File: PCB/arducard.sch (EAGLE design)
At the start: 97 parts, among them J1 USB MICRO, J2 microSD, J3 051296-4094, J4 M02PTH, Q1 BSS84, Q10 DMG2301U-7, Q2 BC817-16LT1SMD, Q3 DMG2301U-7, Q4 2N7002, Q5 BSS84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

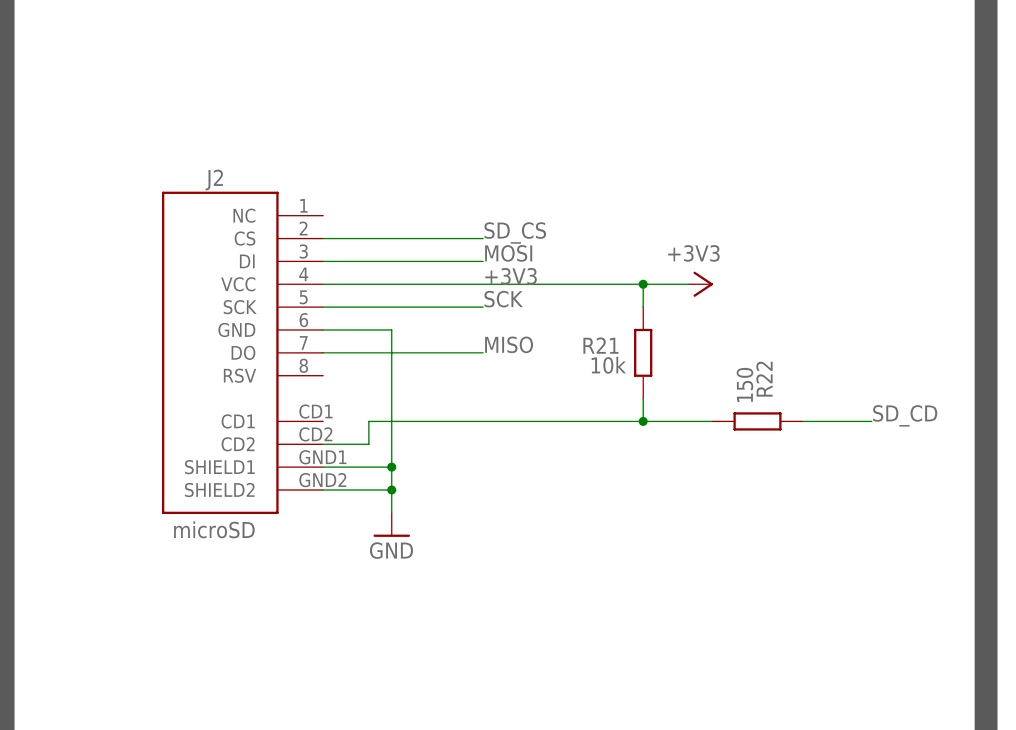
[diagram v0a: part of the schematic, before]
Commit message: removed microsd
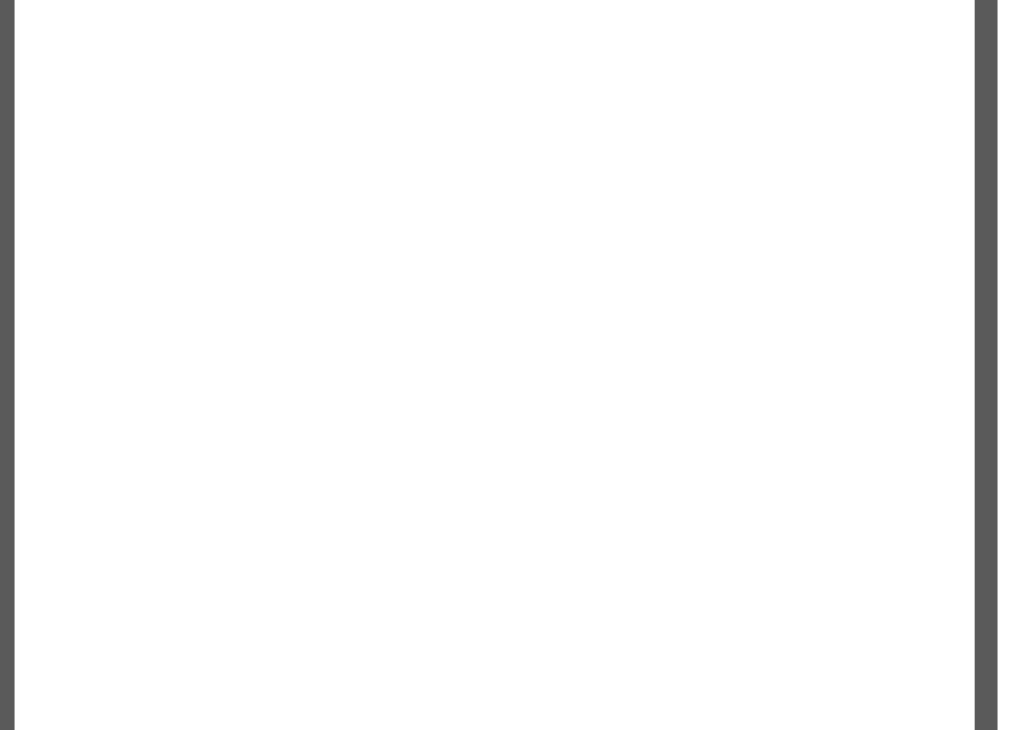
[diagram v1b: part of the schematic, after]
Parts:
- removed J2: microSD, SparkFun:USD-SOCKETSMD
- removed R21: 10k, SmartPrj:R-EU_R0603
- removed R22: 150, SmartPrj:R-EU_R0603
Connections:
- removed net CDP: J2.CD2, R21.1, R22.1
- net +3V3: no longer J2.VCC, R21.2
- net GND: no longer J2.GND, J2.SHIELD1, J2.SHIELD2
- net MISO: no longer J2.DO
- net MOSI: no longer J2.DI
- net SCK: no longer J2.SCK
- net SD_CD: no longer R22.2
- net SD_CS: no longer J2.CS
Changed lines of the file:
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@@
 <part name="+3V3" library="supply1" deviceset="+3V3" device=""/>
 <part name="U1" library="SmartPrj" deviceset="ATMEGA32U4-XU" device="AU"/>
-<part name="J2" library="SparkFun" deviceset="USD-SOCKET" device="SMD" value="microSD"/>
-<part name="R21" library="SmartPrj" deviceset="R-EU_" device="R0603" value="10k"/>
 <part name="C14" library="SmartPrj" deviceset="C-EU" device="C0603" value="1uF"/>
 <part name="+3V4" library="supply1" deviceset="+3V3" device=""/>
@@
 <part name="C11" library="SmartPrj" deviceset="C-EU" device="C0603" value="10 uF"/>
 <part name="+3V5" library="supply1" deviceset="+3V3" device=""/>
-<part name="+3V6" library="supply1" deviceset="+3V3" device=""/>
 <part name="SW0" library="arducard-switch" deviceset="EVQ-PUA" device=""/>
 <part name="R14" library="SmartPrj" deviceset="R-EU_" device="R0603" value="150"/>
@@
 <part name="R17" library="SmartPrj" deviceset="R-EU_" device="R0603" value="150"/>
 <part name="R12" library="SmartPrj" deviceset="R-EU_" device="R0603" value="10k"/>
-<part name="R22" library="SmartPrj" deviceset="R-EU_" device="R0603" value="150"/>
 <part name="C7" library="SmartPrj" deviceset="C-EU" device="C0603" value="100nF"/>
 <part name="C5" library="SmartPrj" deviceset="C-EU" device="C0603" value="1uF"/>
 <part name="GND3" library="supply1" deviceset="GND" device=""/>
 <part name="GND5" library="supply1" deviceset="GND" device=""/>
-<part name="GND7" library="supply1" deviceset="GND" device=""/>
 <part name="GND11" library="supply1" deviceset="GND" device=""/>
 <part name="GND13" library="supply1" deviceset="GND" device=""/>
@@
 <instance part="+3V3" gate="G$1" x="175.26" y="243.84" rot="R270"/>
 <instance part="U1" gate="G$1" x="139.7" y="93.98"/>
-<instance part="J2" gate="G$1" x="627.38" y="241.3" smashed="yes" rot="MR0">
-<attribute name="NAME" x="622.046" y="257.302" size="1.778" layer="95"/>
-<attribute name="VALUE" x="618.236" y="218.186" size="1.778" layer="96"/>
-</instance>
-<instance part="R21" gate="G$1" x="670.56" y="238.76" smashed="yes" rot="R90">
-<attribute name="NAME" x="668.02" y="240.4364" size="1.778" layer="95" rot="R180"/>
-<attribute name="VALUE" x="668.655" y="238.252" size="1.778" layer="96" rot="R180"/>
-</instance>
 <instance part="C14" gate="G$1" x="335.28" y="254"/>
 <instance part="+3V4" gate="G$1" x="45.72" y="142.24"/>
@@
 <instance part="C11" gate="G$1" x="581.66" y="238.76"/>
 <instance part="+3V5" gate="G$1" x="594.36" y="248.92" rot="R270"/>
-<instance part="+3V6" gate="G$1" x="678.18" y="246.38" rot="R270"/>
 <instance part="SW0" gate="G$1" x="60.96" y="264.16"/>
 <instance part="R14" gate="G$1" x="33.02" y="264.16" smashed="yes">
@@
 <attribute name="VALUE" x="60.452" y="230.505" size="1.778" layer="96" rot="R90"/>
 </instance>
-<instance part="R22" gate="G$1" x="683.26" y="231.14" smashed="yes">
-<attribute name="NAME" x="684.9364" y="233.68" size="1.778" layer="95" rot="R90"/>
-<attribute name="VALUE" x="682.752" y="233.045" size="1.778" layer="96" rot="R90"/>
-</instance>
 <instance part="C7" gate="G$1" x="55.88" y="78.74"/>
 <instance part="C5" gate="G$1" x="45.72" y="83.82"/>
 <instance part="GND3" gate="1" x="45.72" y="73.66"/>
 <instance part="GND5" gate="1" x="127" y="228.6" rot="R270"/>
-<instance part="GND7" gate="1" x="642.62" y="218.44"/>
 <instance part="GND11" gate="1" x="546.1" y="228.6"/>
 <instance part="GND13" gate="1" x="581.66" y="228.6"/>
@@
 <pinref part="GND5" gate="1" pin="GND"/>
 <pinref part="U3" gate="G$1" pin="GND"/>
-</segment>
-<segment>
-<pinref part="J2" gate="G$1" pin="GND"/>
-<wire x1="635" y1="241.3" x2="642.62" y2="241.3" width="0.1524" layer="91"/>
-<pinref part="J2" gate="G$1" pin="SHIELD1"/>
-<wire x1="635" y1="226.06" x2="642.62" y2="226.06" width="0.1524" layer="91"/>
-<wire x1="642.62" y1="226.06" x2="642.62" y2="241.3" width="0.1524" layer="91"/>
-<pinref part="J2" gate="G$1" pin="SHIELD2"/>
-<wire x1="635" y1="223.52" x2="642.62" y2="223.52" width="0.1524" layer="91"/>
-<wire x1="642.62" y1="223.52" x2="642.62" y2="226.06" width="0.1524" layer="91"/>
-<junction x="642.62" y="226.06"/>
-<wire x1="642.62" y1="220.98" x2="642.62" y2="223.52" width="0.1524" layer="91"/>
-<junction x="642.62" y="223.52"/>
-<pinref part="GND7" gate="1" pin="GND"/>
 </segment>
 <segment>
@@
 </segment>
 <segment>
-<pinref part="J2" gate="G$1" pin="SCK"/>
-<wire x1="635" y1="243.84" x2="652.78" y2="243.84" width="0.1524" layer="91"/>
-<label x="652.78" y="243.84" size="1.778" layer="95"/>
-</segment>
-<segment>
 <pinref part="U1" gate="G$1" pin="(SCLK/PCINT1)PB1"/>
 <wire x1="175.26" y1="101.6" x2="187.96" y2="101.6" width="0.1524" layer="91"/>
@@
 </segment>
 <segment>
-<pinref part="J2" gate="G$1" pin="DO"/>
-<wire x1="635" y1="238.76" x2="652.78" y2="238.76" width="0.1524" layer="91"/>
-<label x="652.78" y="238.76" size="1.778" layer="95"/>
-</segment>
-<segment>
 <pinref part="U1" gate="G$1" pin="(PD0/MISO/PCINT3)PB3"/>
 <wire x1="175.26" y1="106.68" x2="187.96" y2="106.68" width="0.1524" layer="91"/>
@@
 <label x="175.26" y="228.6" size="1.778" layer="95"/>
 <pinref part="U3" gate="G$1" pin="SI"/>
-</segment>
-<segment>
-<pinref part="J2" gate="G$1" pin="DI"/>
-<wire x1="635" y1="248.92" x2="652.78" y2="248.92" width="0.1524" layer="91"/>
-<label x="652.78" y="248.92" size="1.778" layer="95"/>
 </segment>
 <segment>
@@
 <junction x="574.04" y="248.92"/>
 <pinref part="U2" gate="G1" pin="BYP"/>
-</segment>
-<segment>
-<pinref part="J2" gate="G$1" pin="VCC"/>
-<wire x1="635" y1="246.38" x2="670.56" y2="246.38" width="0.1524" layer="91"/>
-<wire x1="670.56" y1="246.38" x2="670.56" y2="243.84" width="0.1524" layer="91"/>
-<pinref part="R21" gate="G$1" pin="2"/>
-<label x="652.78" y="246.38" size="1.778" layer="95"/>
-<pinref part="+3V6" gate="G$1" pin="+3V3"/>
-<wire x1="670.56" y1="246.38" x2="675.64" y2="246.38" width="0.1524" layer="91"/>
-<junction x="670.56" y="246.38"/>
 </segment>
 <segment>
@@
 </segment>
 </net>
-<net name="CDP" class="0">
-<segment>
-<pinref part="R21" gate="G$1" pin="1"/>
-<wire x1="640.08" y1="231.14" x2="670.56" y2="231.14" width="0.1524" layer="91"/>
-<wire x1="670.56" y1="231.14" x2="678.18" y2="231.14" width="0.1524" layer="91"/>
-<wire x1="670.56" y1="231.14" x2="670.56" y2="233.68" width="0.1524" layer="91"/>
-<junction x="670.56" y="231.14"/>
-<pinref part="R22" gate="G$1" pin="1"/>
-<pinref part="J2" gate="G$1" pin="CD2"/>
-<wire x1="635" y1="228.6" x2="640.08" y2="228.6" width="0.1524" layer="91"/>
-<wire x1="640.08" y1="228.6" x2="640.08" y2="231.14" width="0.1524" layer="91"/>
-</segment>
-</net>
 <net name="SD_CS" class="0">
-<segment>
-<pinref part="J2" gate="G$1" pin="CS"/>
-<wire x1="635" y1="251.46" x2="652.78" y2="251.46" width="0.1524" layer="91"/>
-<label x="652.78" y="251.46" size="1.778" layer="95"/>
-</segment>
 <segment>
 <pinref part="U1" gate="G$1" pin="(XCK1/#CTS)PD5"/>
@@
 <net name="SD_CD" class="0">
 <segment>
-<pinref part="R22" gate="G$1" pin="2"/>
-<wire x1="688.34" y1="231.14" x2="695.96" y2="231.14" width="0.1524" layer="91"/>
-<label x="695.96" y="231.14" size="1.778" layer="95"/>
-</segment>
-<segment>
 <pinref part="U1" gate="G$1" pin="(PCINT5/OC1A/#OC4B/ADC12)PB5"/>

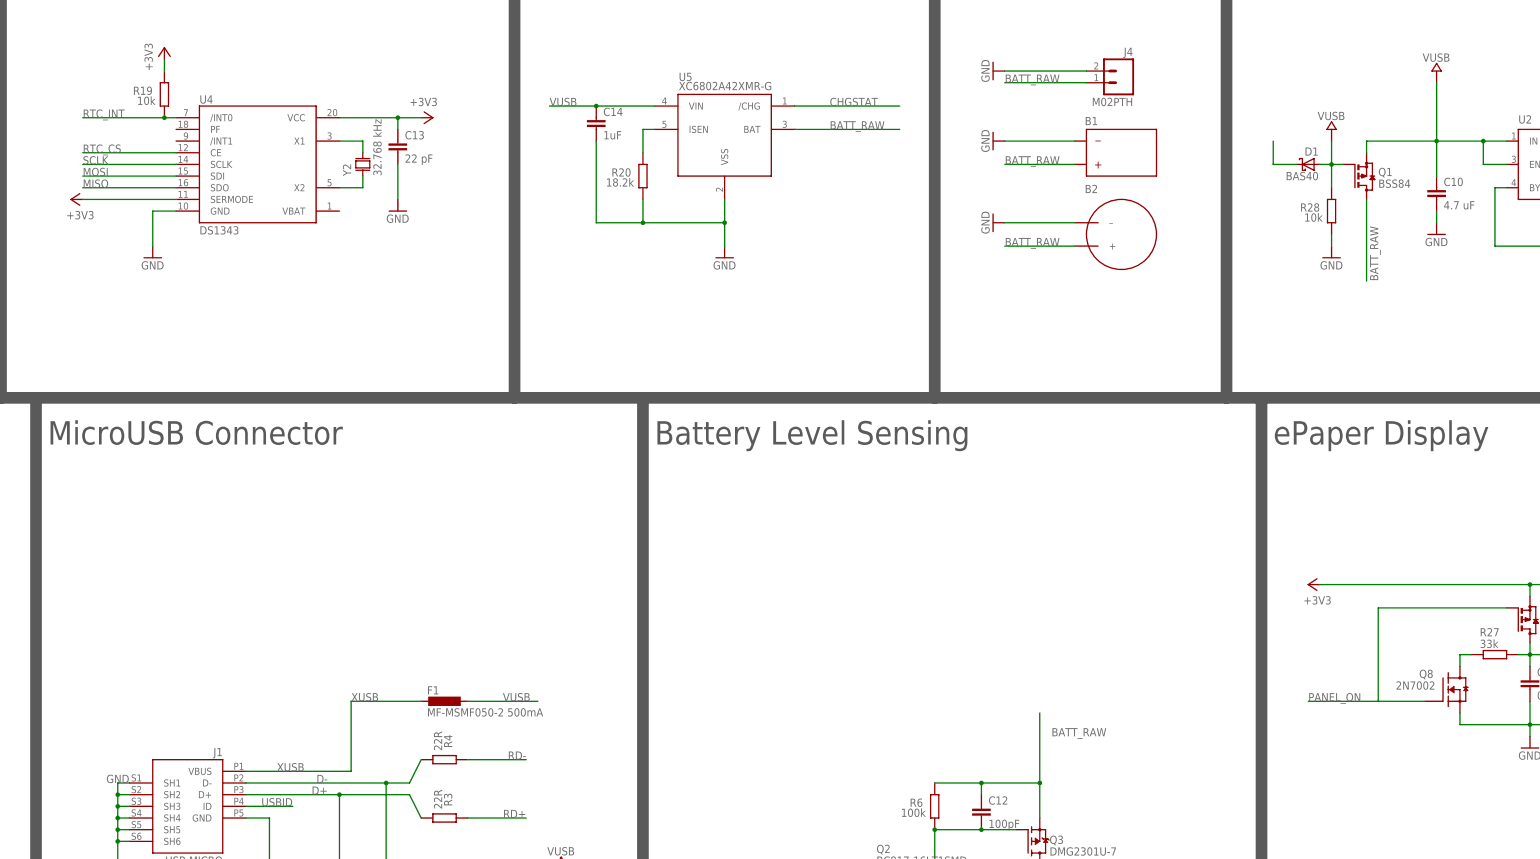
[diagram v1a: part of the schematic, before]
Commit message: fixed VUSB diode
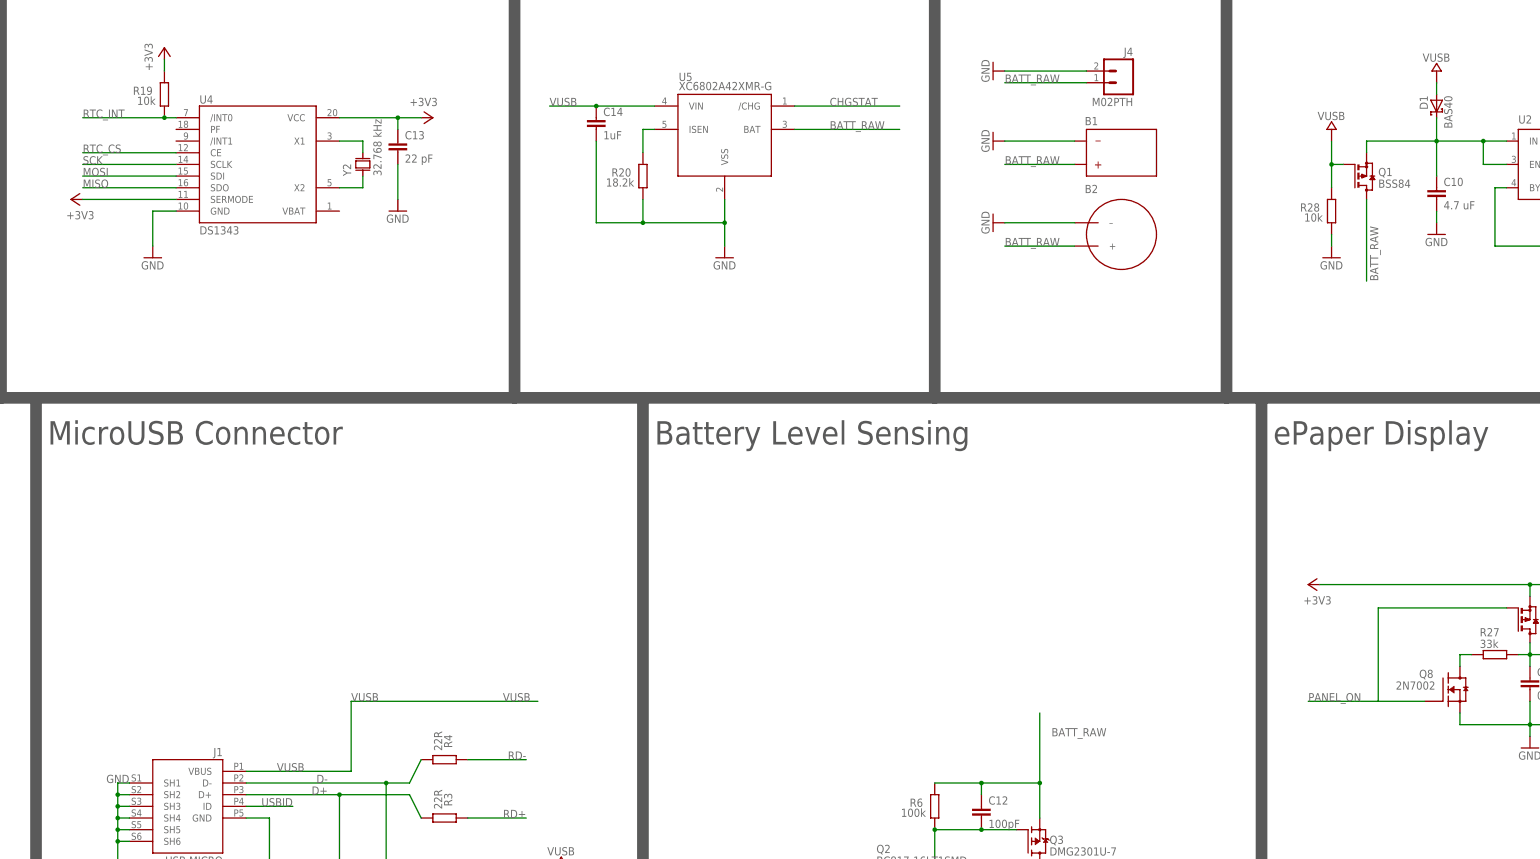
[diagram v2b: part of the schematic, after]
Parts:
- removed F1: MF-MSMF050-2 500mA, rcl:L-EUL1812
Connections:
- removed net SCLK: U4.SCLK
- removed net XUSB: F1.2, J1.VBUS
- net N$10: now also C10.1, Q1.S, U2.EN, U2.IN
- net SCK: now also U4.SCLK
- net VUSB: now also J1.VBUS; no longer C10.1, F1.1, Q1.S, U2.EN, U2.IN
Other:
- moved on the sheet: D1
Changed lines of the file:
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@@
 <part name="GND18" library="supply1" deviceset="GND" device=""/>
 <part name="Y1" library="SmartPrj" deviceset="CRYSTAL-3.2-2.5" device="" value="8MHz KX-7"/>
-<part name="F1" library="rcl" deviceset="L-EU" device="L1812" value="MF-MSMF050-2 500mA"/>
 <part name="Z1" library="varistor" deviceset="VARISTOR" device="CN0603" value="CG0603MLC-05E"/>
 <part name="Z2" library="varistor" deviceset="VARISTOR" device="CN0603" value="CG0603MLC-05E"/>
@@
 <attribute name="VALUE" x="38.1" y="96.52" size="1.778" layer="96"/>
 </instance>
-<instance part="F1" gate="G$1" x="302.26" y="127" rot="R270"/>
 <instance part="Z1" gate="G$1" x="279.4" y="76.2" smashed="yes" rot="R90">
 <attribute name="NAME" x="276.86" y="73.66" size="1.778" layer="95" rot="R90"/>
@@
 <instance part="Q1" gate="G$1" x="502.92" y="241.3"/>
 <instance part="U$12" gate="G$1" x="518.16" y="264.16"/>
-<instance part="D1" gate="1" x="490.22" y="243.84" rot="MR0"/>
+<instance part="D1" gate="1" x="518.16" y="256.54" rot="MR270"/>
 <instance part="U3" gate="G$1" x="152.4" y="238.76"/>
 <instance part="U5" gate="XC6802A42XMR-G" x="363.22" y="254"/>
@@
 <pinref part="J3" gate="G$1" pin="SCLK"/>
 </segment>
+<segment>
+<pinref part="U4" gate="G$1" pin="SCLK"/>
+<wire x1="243.84" y1="243.84" x2="223.52" y2="243.84" width="0.1524" layer="91"/>
+<label x="223.52" y="243.84" size="1.778" layer="95"/>
+</segment>
 </net>
 <net name="MISO" class="0">
@@
 </segment>
 </net>
-<net name="VUSB" class="0">
+<net name="VUSB" class="3">
 <segment>
 <wire x1="114.3" y1="60.96" x2="104.14" y2="60.96" width="0.1524" layer="91"/>
@@
 </segment>
 <segment>
-<wire x1="322.58" y1="127" x2="307.34" y2="127" width="0.1524" layer="91"/>
-<label x="314.96" y="127" size="1.778" layer="95"/>
-<pinref part="F1" gate="G$1" pin="1"/>
-</segment>
-<segment>
 <wire x1="347.98" y1="256.54" x2="335.28" y2="256.54" width="0.1524" layer="91"/>
 <pinref part="C14" gate="G$1" pin="1"/>
@@
 </segment>
 <segment>
-<wire x1="528.32" y1="248.92" x2="533.4" y2="248.92" width="0.1524" layer="91"/>
-<wire x1="533.4" y1="243.84" x2="528.32" y2="243.84" width="0.1524" layer="91"/>
-<wire x1="528.32" y1="243.84" x2="528.32" y2="248.92" width="0.1524" layer="91"/>
-<wire x1="528.32" y1="248.92" x2="518.16" y2="248.92" width="0.1524" layer="91"/>
-<junction x="528.32" y="248.92"/>
-<pinref part="C10" gate="G$1" pin="1"/>
-<wire x1="518.16" y1="241.3" x2="518.16" y2="248.92" width="0.1524" layer="91"/>
-<junction x="518.16" y="248.92"/>
-<pinref part="U$12" gate="G$1" pin="VUSB"/>
-<wire x1="518.16" y1="248.92" x2="518.16" y2="261.62" width="0.1524" layer="91"/>
-<pinref part="U2" gate="G1" pin="IN"/>
-<pinref part="U2" gate="G1" pin="EN"/>
-<pinref part="Q1" gate="G$1" pin="S"/>
-<wire x1="502.92" y1="246.38" x2="502.92" y2="248.92" width="0.1524" layer="91"/>
-<wire x1="502.92" y1="248.92" x2="518.16" y2="248.92" width="0.1524" layer="91"/>
-</segment>
-<segment>
-<pinref part="D1" gate="1" pin="A"/>
 <pinref part="Q1" gate="G$1" pin="G"/>
-<wire x1="492.76" y1="243.84" x2="495.3" y2="243.84" width="0.1524" layer="91"/>
 <pinref part="R28" gate="G$1" pin="2"/>
 <wire x1="495.3" y1="243.84" x2="497.84" y2="243.84" width="0.1524" layer="91"/>
@@
 <wire x1="495.3" y1="243.84" x2="495.3" y2="248.92" width="0.1524" layer="91"/>
 <junction x="495.3" y="243.84"/>
+</segment>
+<segment>
+<pinref part="D1" gate="1" pin="A"/>
+<pinref part="U$12" gate="G$1" pin="VUSB"/>
+<wire x1="518.16" y1="259.08" x2="518.16" y2="261.62" width="0.1524" layer="91"/>
+</segment>
+<segment>
+<wire x1="281.94" y1="111.76" x2="281.94" y2="127" width="0.1524" layer="91"/>
+<wire x1="281.94" y1="127" x2="322.58" y2="127" width="0.1524" layer="91"/>
+<wire x1="259.08" y1="111.76" x2="281.94" y2="111.76" width="0.1524" layer="91"/>
+<label x="271.78" y="111.76" size="1.778" layer="95" rot="MR0"/>
+<label x="281.94" y="127" size="1.778" layer="95"/>
+<pinref part="J1" gate="G$1" pin="VBUS"/>
+<label x="314.96" y="127" size="1.778" layer="95"/>
 </segment>
 </net>
@@
 <pinref part="J1" gate="G$1" pin="D+"/>
 <pinref part="R3" gate="G$1" pin="1"/>
-</segment>
-</net>
-<net name="XUSB" class="3">
-<segment>
-<wire x1="281.94" y1="111.76" x2="281.94" y2="127" width="0.1524" layer="91"/>
-<wire x1="281.94" y1="127" x2="297.18" y2="127" width="0.1524" layer="91"/>
-<wire x1="259.08" y1="111.76" x2="281.94" y2="111.76" width="0.1524" layer="91"/>
-<label x="271.78" y="111.76" size="1.778" layer="95" rot="MR0"/>
-<label x="281.94" y="127" size="1.778" layer="95"/>
-<pinref part="F1" gate="G$1" pin="2"/>
-<pinref part="J1" gate="G$1" pin="VBUS"/>
 </segment>
 </net>
@@
 </segment>
 </net>
-<net name="SCLK" class="0">
-<segment>
-<pinref part="U4" gate="G$1" pin="SCLK"/>
-<wire x1="243.84" y1="243.84" x2="223.52" y2="243.84" width="0.1524" layer="91"/>
-<label x="223.52" y="243.84" size="1.778" layer="95"/>
-</segment>
-</net>
 <net name="N$10" class="0">
 <segment>
-<wire x1="482.6" y1="248.92" x2="482.6" y2="243.84" width="0.1524" layer="91"/>
+<wire x1="528.32" y1="248.92" x2="533.4" y2="248.92" width="0.1524" layer="91"/>
+<wire x1="533.4" y1="243.84" x2="528.32" y2="243.84" width="0.1524" layer="91"/>
+<wire x1="528.32" y1="243.84" x2="528.32" y2="248.92" width="0.1524" layer="91"/>
+<wire x1="528.32" y1="248.92" x2="518.16" y2="248.92" width="0.1524" layer="91"/>
+<junction x="528.32" y="248.92"/>
+<pinref part="C10" gate="G$1" pin="1"/>
+<wire x1="518.16" y1="241.3" x2="518.16" y2="248.92" width="0.1524" layer="91"/>
+<junction x="518.16" y="248.92"/>
+<pinref part="U2" gate="G1" pin="IN"/>
+<pinref part="U2" gate="G1" pin="EN"/>
+<pinref part="Q1" gate="G$1" pin="S"/>
+<wire x1="502.92" y1="246.38" x2="502.92" y2="248.92" width="0.1524" layer="91"/>
+<wire x1="502.92" y1="248.92" x2="518.16" y2="248.92" width="0.1524" layer="91"/>
 <pinref part="D1" gate="1" pin="C"/>
-<wire x1="482.6" y1="243.84" x2="487.68" y2="243.84" width="0.1524" layer="91"/>
-</segment>
-</net>
+<wire x1="518.16" y1="254" x2="518.16" y2="248.92" width="0.1524" layer="91"/>
+</segment>
+</net>
